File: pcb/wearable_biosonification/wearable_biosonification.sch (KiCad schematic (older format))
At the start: 16 parts, among them J1 Electrodes, J2 1.5V, U1 LM324

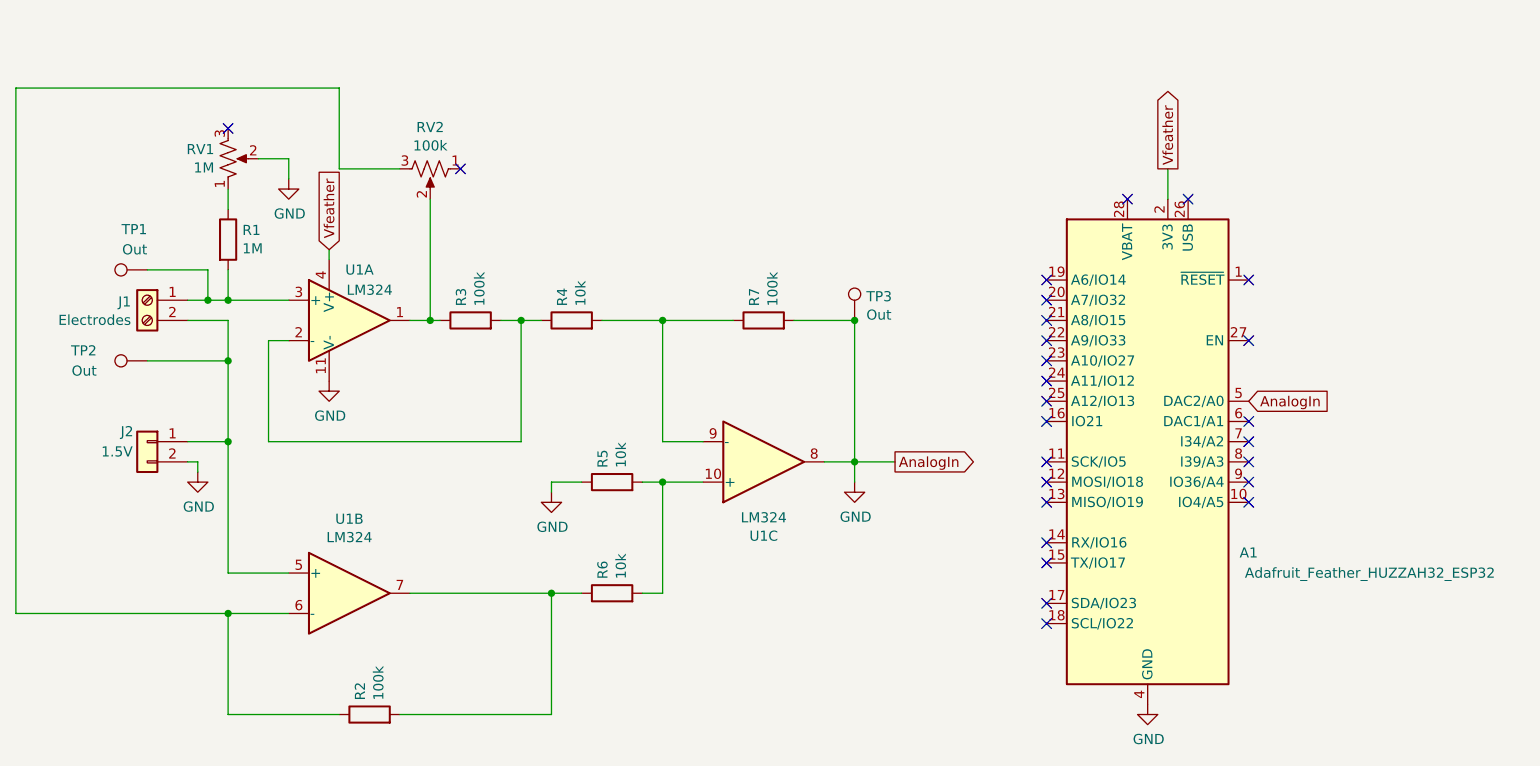
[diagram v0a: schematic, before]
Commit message: removed testpoints + added LED
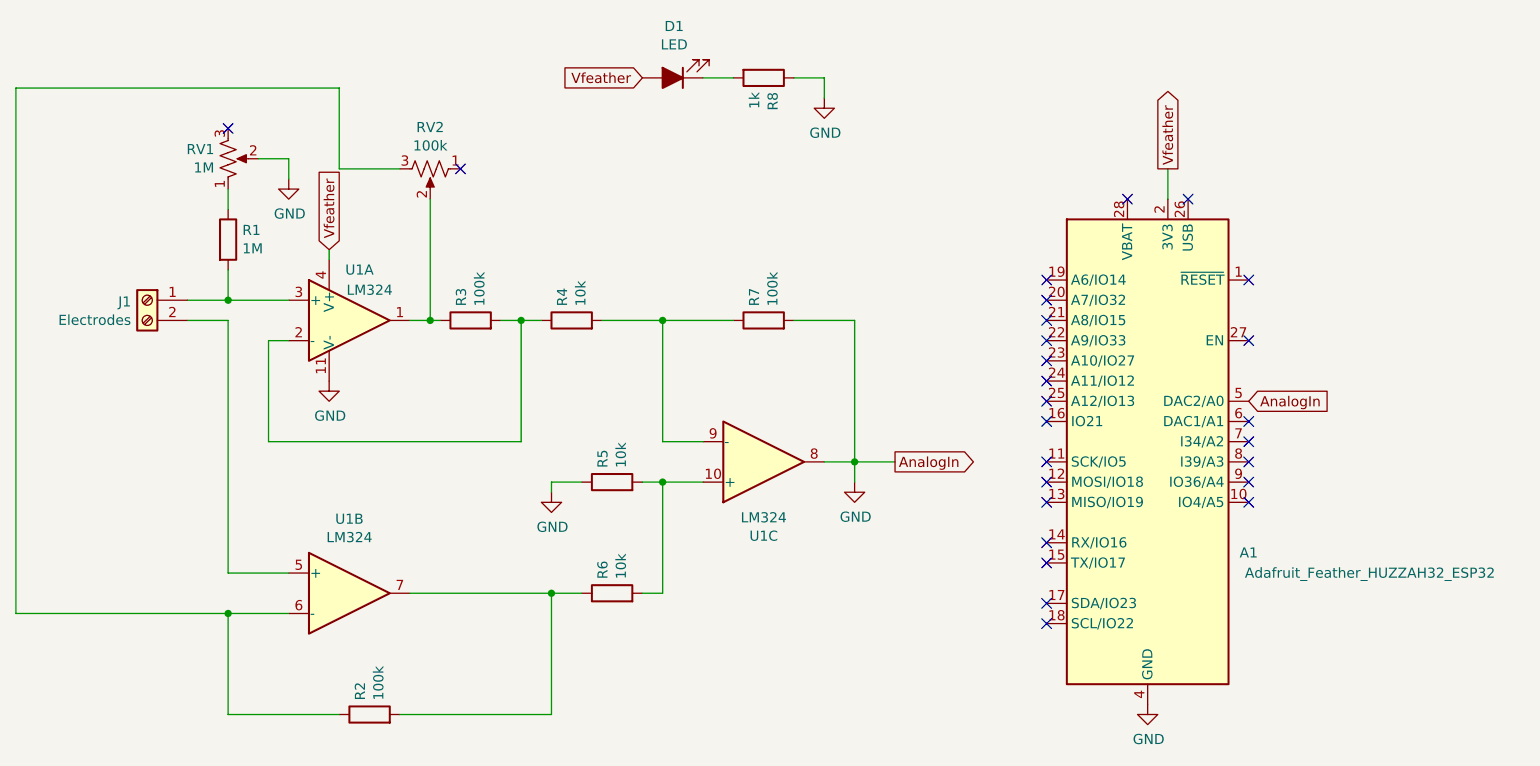
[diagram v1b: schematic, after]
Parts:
- removed J2: 1.5V, Connector_PinHeader_2.54mm:PinHeader_1x02_P2.54mm_Vertical, symbol Connector_Generic:Conn_01x02
- removed TP1, TP2, TP3: Out, TestPoint:TestPoint_THTPad_D2.0mm_Drill1.0mm, symbol Connector:TestPoint
- added D1: LED, LED_SMD:LED_0805_2012Metric_Pad1.15x1.40mm_HandSolder, symbol Device:LED_ALT
- added R8: 1k, Resistor_SMD:R_0805_2012Metric_Pad1.20x1.40mm_HandSolder, symbol Device:R
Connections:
- net GND: now also R8.1
- net Vfeather: now also D1.2 (A)
- new net: D1.1 (K), R8.2
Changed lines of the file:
@@
 $EndComp
-Wire Wire Line
-	1850 3650 1950 3650
 Wire Wire Line
 	2050 3650 2050 3500
@@
 Wire Wire Line
 	2050 5000 2350 5000
-Wire Wire Line
-	2050 3750 2050 3950
 Wire Wire Line
 	3400 3750 3500 3750
@@
 	2950 5100 3650 5100
 Connection ~ 3650 5100
-$Comp
-L Connector:TestPoint TP3
-U 1 1 5FF4621A
-P 5150 3750
-F 0 "TP3" H 5208 3868 50  0000 L CNN
-F 1 "Out" H 5208 3777 50  0000 L CNN
-F 2 "TestPoint:TestPoint_THTPad_D2.0mm_Drill1.0mm" H 5350 3750 50  0001 C CNN
-F 3 "~" H 5350 3750 50  0001 C CNN
-	1    5150 3750
-	1    0    0    -1
-$EndComp
-Connection ~ 5150 3750
-$Comp
-L Connector:TestPoint TP1
-U 1 1 5FF800DD
-P 1650 3500
-F 0 "TP1" V 1850 3500 50  0000 L CNN
-F 1 "Out" V 1750 3500 50  0000 L CNN
-F 2 "TestPoint:TestPoint_THTPad_D2.0mm_Drill1.0mm" H 1850 3500 50  0001 C CNN
-F 3 "~" H 1850 3500 50  0001 C CNN
-	1    1650 3500
-	0    -1   -1   0
-$EndComp
-$Comp
-L Connector:TestPoint TP2
-U 1 1 5FF8122F
-P 1650 3950
-F 0 "TP2" V 1700 4200 50  0000 L CNN
-F 1 "Out" V 1600 4200 50  0000 L CNN
-F 2 "TestPoint:TestPoint_THTPad_D2.0mm_Drill1.0mm" H 1850 3950 50  0001 C CNN
-F 3 "~" H 1850 3950 50  0001 C CNN
-	1    1650 3950
-	0    -1   -1   0
-$EndComp
-Wire Wire Line
-	1650 3950 2050 3950
-Connection ~ 2050 3950
-Wire Wire Line
-	1650 3500 1950 3500
-Wire Wire Line
-	1950 3500 1950 3650
-Connection ~ 1950 3650
-Wire Wire Line
-	1950 3650 2050 3650
 NoConn ~ 3200 3000
 NoConn ~ 2050 2800
@@
 	2550 3400 2550 3450
 Wire Wire Line
-	2050 3950 2050 4350
-$Comp
-L Connector_Generic:Conn_01x02 J2
-U 1 1 5FCEBE87
-P 1650 4350
-F 0 "J2" H 1750 4400 50  0000 C CNN
-F 1 "1.5V" H 1800 4300 50  0000 C CNN
-F 2 "Connector_PinHeader_2.54mm:PinHeader_1x02_P2.54mm_Vertical" H 1650 4350 50  0001 C CNN
-F 3 "~" H 1650 4350 50  0001 C CNN
-	1    1650 4350
-	-1   0    0    -1
-$EndComp
-$Comp
-L power:GND #PWR0101
-U 1 1 5FCF9E94
-P 1900 4500
-F 0 "#PWR0101" H 1900 4250 50  0001 C CNN
-F 1 "GND" H 1905 4327 50  0000 C CNN
-F 2 "" H 1900 4500 50  0001 C CNN
-F 3 "" H 1900 4500 50  0001 C CNN
-	1    1900 4500
-	1    0    0    -1
-$EndComp
-Wire Wire Line
-	1850 4350 2050 4350
-Connection ~ 2050 4350
-Wire Wire Line
-	2050 4350 2050 5000
-Wire Wire Line
-	1850 4450 1900 4450
-Wire Wire Line
-	1900 4450 1900 4500
+	1850 3650 2050 3650
+$Comp
+L Device:R R8
+U 1 1 5FD1634A
+P 4700 2550
+F 0 "R8" H 4770 2596 50  0000 L CNN
+F 1 "1k" H 4770 2505 50  0000 L CNN
+F 2 "Resistor_SMD:R_0805_2012Metric_Pad1.20x1.40mm_HandSolder" V 4630 2550 50  0001 C CNN
+F 3 "~" H 4700 2550 50  0001 C CNN
+	1    4700 2550
+	0    1    1    0
+$EndComp
+$Comp
+L Device:LED_ALT D1
+U 1 1 5FD1F003
+P 4250 2550
+F 0 "D1" H 4243 2295 50  0000 C CNN
+F 1 "LED" H 4243 2386 50  0000 C CNN
+F 2 "LED_SMD:LED_0805_2012Metric_Pad1.15x1.40mm_HandSolder" H 4250 2550 50  0001 C CNN
+F 3 "~" H 4250 2550 50  0001 C CNN
+	1    4250 2550
+	-1   0    0    1
+$EndComp
+Wire Wire Line
+	4400 2550 4550 2550
+Text GLabel 4100 2550 0    50   Input ~ 0
+Vfeather
+$Comp
+L power:GND #PWR01
+U 1 1 5FD35904
+P 5000 2650
+F 0 "#PWR01" H 5000 2400 50  0001 C CNN
+F 1 "GND" H 5005 2477 50  0000 C CNN
+F 2 "" H 5000 2650 50  0001 C CNN
+F 3 "" H 5000 2650 50  0001 C CNN
+	1    5000 2650
+	1    0    0    -1
+$EndComp
+Wire Wire Line
+	4850 2550 5000 2550
+Wire Wire Line
+	5000 2550 5000 2650
+Wire Wire Line
+	2050 3750 2050 5000
 $EndSCHEMATC
